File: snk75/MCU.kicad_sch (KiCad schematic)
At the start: 2 parts, among them U4 STM32F072C8Tx

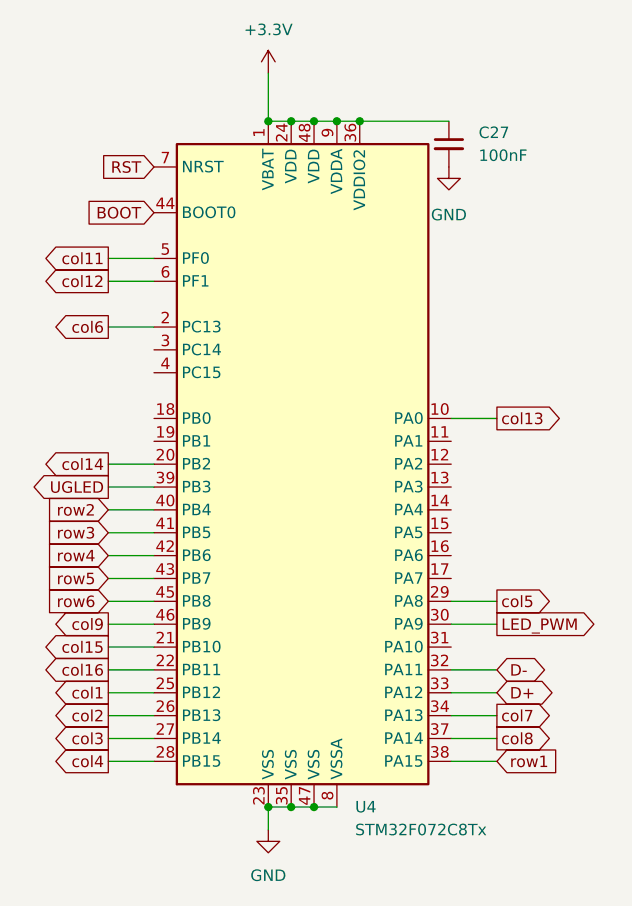
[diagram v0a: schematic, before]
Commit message: added new row layout and connected row1 to MCU
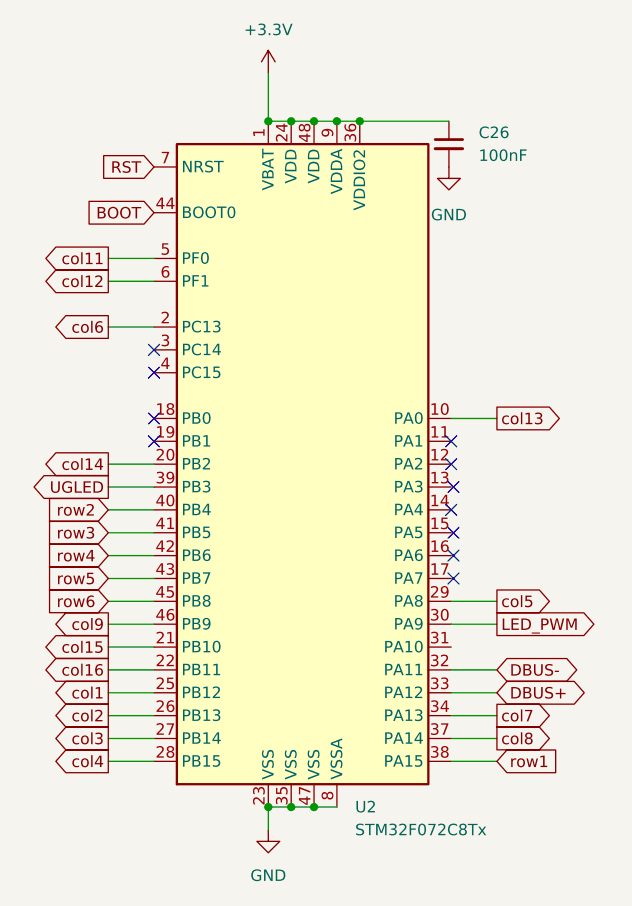
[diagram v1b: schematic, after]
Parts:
- C26: renamed from C27; footprint (none) -> Capacitor_SMD:C_0402_1005Metric
- renumbered U4 to U2
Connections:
- net D+ renamed DBUS+
- net D- renamed DBUS-
- no-connect marks 0 -> 11
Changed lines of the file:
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@@
   (junction (at 147.32 58.42) (diameter 0) (color 0 0 0 0)
   )
+  (no_connect (at 124.46 93.98))
+  (no_connect (at 157.48 101.6))
+  (no_connect (at 124.46 86.36))
+  (no_connect (at 124.46 83.82))
+  (no_connect (at 157.48 96.52))
+  (no_connect (at 157.734 99.06))
+  (no_connect (at 157.734 109.22))
+  (no_connect (at 157.734 104.14))
+  (no_connect (at 157.48 93.98))
+  (no_connect (at 124.46 91.44))
+  (no_connect (at 157.734 106.68))
   (wire (pts (xy 119.38 129.54) (xy 124.46 129.54))
     (stroke (width 0) (type default) (color 0 0 0 0))
@@
     )
   )
-  (global_label "D-" (shape bidirectional) (at 162.56 119.38 0) (fields_autoplaced)
-    (effects (font (size 1.27 1.27)) (justify left))
-    (property "Intersheet References" "${INTERSHEET_REFS}" (id 0) (at 167.8155 119.3006 0)
+  (global_label "DBUS-" (shape bidirectional) (at 162.56 119.38 0) (fields_autoplaced)
+    (effects (font (size 1.27 1.27)) (justify left))
+    (property "Intersheet References" "${INTERSHEET_REFS}" (id 0) (at 171.6255 119.3006 0)
       (effects (font (size 1.27 1.27)) (justify left) hide)
     )
@@
     )
   )
-  (global_label "D+" (shape bidirectional) (at 162.56 121.92 0) (fields_autoplaced)
-    (effects (font (size 1.27 1.27)) (justify left))
-    (property "Intersheet References" "${INTERSHEET_REFS}" (id 0) (at 167.8155 121.9994 0)
+  (global_label "DBUS+" (shape bidirectional) (at 162.56 121.92 0) (fields_autoplaced)
+    (effects (font (size 1.27 1.27)) (justify left))
+    (property "Intersheet References" "${INTERSHEET_REFS}" (id 0) (at 171.6255 121.8406 0)
       (effects (font (size 1.27 1.27)) (justify left) hide)
     )
@@
   (symbol (lib_id "Device:C_Small") (at 157.226 60.96 0) (unit 1)
     (in_bom yes) (on_board yes) (fields_autoplaced)
-    (property "Reference" "C27" (id 0) (at 160.528 59.6962 0)
+    (property "Reference" "C26" (id 0) (at 160.528 59.6962 0)
       (effects (font (size 1.27 1.27)) (justify left))
     )
@@
       (effects (font (size 1.27 1.27)) (justify left))
     )
-    (property "Footprint" "" (id 2) (at 157.226 60.96 0)
+    (property "Footprint" "Capacitor_SMD:C_0402_1005Metric" (id 2) (at 157.226 60.96 0)
       (effects (font (size 1.27 1.27)) hide)
     )
@@
   (symbol (lib_id "MCU_ST_STM32F0:STM32F072C8Tx") (at 142.24 96.52 0) (unit 1)
     (in_bom yes) (on_board yes) (fields_autoplaced)
-    (property "Reference" "U4" (id 0) (at 146.7994 134.62 0)
+    (property "Reference" "U2" (id 0) (at 146.7994 134.62 0)
       (effects (font (size 1.27 1.27)) (justify left))
     )
@@
   (symbol (lib_id "power:+3.3V") (at 137.16 53.086 0) (unit 1)
     (in_bom yes) (on_board yes) (fields_autoplaced)
-    (property "Reference" "#PWR023" (id 0) (at 137.16 56.896 0)
+    (property "Reference" "#PWR045" (id 0) (at 137.16 56.896 0)
       (effects (font (size 1.27 1.27)) hide)
     )
@@
   (symbol (lib_id "power:GND") (at 157.226 63.5 0) (unit 1)
     (in_bom yes) (on_board yes) (fields_autoplaced)
-    (property "Reference" "#PWR025" (id 0) (at 157.226 69.85 0)
+    (property "Reference" "#PWR047" (id 0) (at 157.226 69.85 0)
       (effects (font (size 1.27 1.27)) hide)
     )
@@
   (symbol (lib_id "power:GND") (at 137.16 137.16 0) (unit 1)
     (in_bom yes) (on_board yes) (fields_autoplaced)
-    (property "Reference" "#PWR024" (id 0) (at 137.16 143.51 0)
-      (effects (font (size 1.27 1.27)) hide)
-    )
+    (property "Reference" "#PWR046" (id 0) (at 137.16 143.51 0)
+      (effects (font (size 1.27 1.27)) hide)
+    )
